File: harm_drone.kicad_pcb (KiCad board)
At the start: 2 copper layers, 90 x 40 mm, 0 parts

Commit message: initial PCB draft!
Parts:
- added C1: 0.1uF, Capacitor_SMD:C_0805_2012Metric, F.Cu at (131.9, 96.5)
- added C10: 22uF, Capacitor_SMD:C_0805_2012Metric, F.Cu at (112.4, 86.0)
- added C11: 22uF, Capacitor_SMD:C_0805_2012Metric, F.Cu at (112.4, 89.0)
- added C12: 47pF, Capacitor_SMD:C_0805_2012Metric, F.Cu at (116.9, 84.5)
- added C13: 47pF, Capacitor_SMD:C_0805_2012Metric, F.Cu at (116.9, 87.5)
- added C14: 1uF, Capacitor_SMD:C_0805_2012Metric, F.Cu at (116.9, 90.5)
- added C15: 10uF, Capacitor_SMD:C_0805_2012Metric, F.Cu at (131.9, 99.1)
- added C16: 0.1uF, Capacitor_SMD:C_0805_2012Metric, F.Cu at (132.0, 101.5)
- added C17: 0.1uF, Capacitor_SMD:C_0805_2012Metric, F.Cu at (140.9, 105.5)
- added C18: 10uF, Capacitor_SMD:C_0805_2012Metric, F.Cu at (143.4, 105.5)
- added C19: 10uF, Capacitor_SMD:C_0805_2012Metric, F.Cu at (144.4, 90.5)
- added C2: 10uF, Capacitor_SMD:C_0805_2012Metric, F.Cu at (180.4, 95.0)
- added C20: 0.1uF, Capacitor_SMD:C_0805_2012Metric, F.Cu at (141.9, 90.5)
- added C21: 10uF, Capacitor_SMD:C_0805_2012Metric, F.Cu at (135.4, 90.5)
- added C22: 0.1uF, Capacitor_SMD:C_0805_2012Metric, F.Cu at (137.9, 90.5)
- added C23: 10uF, Capacitor_SMD:C_0805_2012Metric, F.Cu at (186.4, 113.0)
- added C24: 0.1uF, Capacitor_SMD:C_0805_2012Metric, F.Cu at (186.4, 116.0)
- added C3: 0.1uF, Capacitor_SMD:C_0805_2012Metric, F.Cu at (180.4, 98.0)
- added C4: 0.1uF, Capacitor_SMD:C_0805_2012Metric, F.Cu at (180.4, 101.0)
- added C5: 10uF, Capacitor_SMD:C_0805_2012Metric, F.Cu at (180.4, 104.0)
- added C6: 1uF, Capacitor_SMD:C_0805_2012Metric, F.Cu at (128.9, 83.0)
- added C7: 1uF, Capacitor_SMD:C_0805_2012Metric, F.Cu at (128.9, 86.0)
- added C8: 0.1uFCap, Capacitor_SMD:C_0805_2012Metric, F.Cu at (112.4, 80.0)
- added C9: 0.1uF, Capacitor_SMD:C_0805_2012Metric, F.Cu at (112.4, 83.0)
- added IC1: Microcontroller, group127:Microcontroller, F.Cu at (139.4, 98.0)
- added IC2: USB Hub, group127:USB-HUB, F.Cu at (171.9, 100.5)
- added IC3: SRAM, group127:SRAM, F.Cu at (157.8, 98.6)
- added IC4: LDO, group127:LDO, F.Cu at (130.3, 90.0)
- added J1: SYS_DEBUG, Connector_PinHeader_2.54mm:PinHeader_1x03_P2.54mm_Vertical, F.Cu at (149.4, 88.5)
- added J2: 2-Port USB, group127:USBPorts, F.Cu at (155.9, 110.8)
- added J3: 2-Port USB, group127:USBPorts, F.Cu at (172.4, 110.8)
- added J4: SD_Card, group127:SDCard, F.Cu at (196.9, 110.0)
- added J5: SPI2, Connector_PinHeader_2.54mm:PinHeader_1x04_P2.54mm_Vertical, F.Cu at (149.4, 106.0)
- added J6: SPI1, Connector_PinHeader_2.54mm:PinHeader_1x05_P2.54mm_Vertical, F.Cu at (144.4, 109.0)
- added J7: XT60-M, group127:XT60-M, F.Cu at (157.0, 86.9)
- added L1: 6.8uH, group127:Inductor, F.Cu at (102.9, 86.5)
- added R1: 2kOhm, Resistor_SMD:R_0805_2012Metric, F.Cu at (169.9, 93.0)
- added R10: 27ohm, Resistor_SMD:R_0805_2012Metric, F.Cu at (110.4, 100.5)
- added R11: 27ohm, Resistor_SMD:R_0805_2012Metric, F.Cu at (110.4, 103.5)
- added R12: 270ohm, Resistor_SMD:R_0805_2012Metric, F.Cu at (110.4, 106.5)
- added R13: 270ohm, Resistor_SMD:R_0805_2012Metric, F.Cu at (110.4, 109.4)
- added R14: 5.1kohm, Resistor_SMD:R_0805_2012Metric, F.Cu at (110.4, 112.3)
- added R15: 5.1kohm, Resistor_SMD:R_0805_2012Metric, F.Cu at (110.4, 115.3)
- added R2: 100k, Resistor_SMD:R_0805_2012Metric, F.Cu at (112.4, 92.0)
- added R3: 13.7k, Resistor_SMD:R_0805_2012Metric, F.Cu at (112.4, 94.9)
- added R4: 10kOhm, Resistor_SMD:R_0805_2012Metric, F.Cu at (198.9, 82.0)
- added R5: 10kOhm, Resistor_SMD:R_0805_2012Metric, F.Cu at (198.9, 85.0)
- added R6: 27, Resistor_SMD:R_0805_2012Metric, F.Cu at (198.9, 88.0)
- added R7: 10kOhm, Resistor_SMD:R_0805_2012Metric, F.Cu at (198.9, 90.9)
- added R8: 10kOhm, Resistor_SMD:R_0805_2012Metric, F.Cu at (198.9, 93.8)
- added R9: 10kOhm, Resistor_SMD:R_0805_2012Metric, F.Cu at (198.9, 96.8)
- added RXLED1: SM0805UBWC, KiCad0805:LEDC2012X110N, F.Cu at (118.4, 95.5)
- added S1: KSR221GLFS, group127:Button, F.Cu at (125.4, 99.7)
- added S2: Switch, JS102011SAQN:SW_JS102011SAQN, F.Cu at (138.9, 118.0)
- added TXLED1: SM0805UBWC, KiCad0805:LEDC2012X110N, F.Cu at (118.4, 98.8)
- added U1: LMR51430, Package_TO_SOT_SMD:SOT-23-6, F.Cu at (103.8, 96.5)
- added U2: EEPROM, group127:EEPROM, F.Cu at (157.8, 105.1)
- added USB-C1: USB4110GFA, USB4110_GF_A:GCT_USB4110GFA, F.Cu at (121.4, 113.9)
- added USB2UART1: FT231XS-R, Package_SO:SSOP-20_3.9x8.7mm_P0.635mm, F.Cu at (122.8, 87.6)
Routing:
- net GND: vias 0 -> 9
- net 3V3: vias 0 -> 8
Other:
- board size 90 x 40 mm -> 110 x 40 mm
- copper layers 2 -> 4

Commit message: before differential routing
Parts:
- C8: value 0.1uFCap -> 0.1uF
- moved C11 73.9 mm to (186.0, 82.0), turned to 90 degrees
- moved R2 70.9 mm to (183.0, 86.0), turned to 90 degrees
- moved R3 70.8 mm to (183.0, 90.0), turned to -90 degrees
- moved C10 70.7 mm to (183.0, 82.0), turned to 90 degrees
- moved L1 70.6 mm to (173.5, 85.5), turned to 180 degrees
- moved U1 61.1 mm to (164.0, 86.5)
- moved C6 52.5 mm to (178.0, 101.5)
- moved C8 52.2 mm to (163.0, 93.0), turned to 90 degrees
- moved C9 51.6 mm to (164.0, 82.5), turned to 180 degrees
- moved C7 49.8 mm to (178.0, 94.5)
- moved IC4 48.3 mm to (178.0, 98.0), turned to 90 degrees
- moved C2 32.2 mm to (149.5, 104.0), turned to 180 degrees
- moved C3 31.1 mm to (149.5, 101.5), turned to 180 degrees
- moved IC3 27.7 mm to (135.5, 115.0)
- moved R6 25.7 mm to (186.5, 110.5)
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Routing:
- net 5V: track 0.00 -> 59.7 mm
- net Net-(J7-POS): track 0.00 -> 6.64 mm
- net Net-(IC2-BUSPWR): track 0.00 -> 3.09 mm
- net GND: vias 9 -> 15
- net DP0: vias 0 -> 1
- net DM0: vias 0 -> 1
- net 3V3: vias 8 -> 14
- net /USB/DP4: vias 0 -> 1
- net /USB/DP3: vias 0 -> 1
- net /USB/DP2: vias 0 -> 1
- net /USB/DP1: vias 0 -> 1
- net /USB/DM4: vias 0 -> 1
- net /USB/DM3: vias 0 -> 1
- net /USB/DM2: vias 0 -> 1
- net /USB/DM1: vias 0 -> 1

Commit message: namespace change
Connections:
- net /USB/DM1 renamed /USB/D1-
- net /USB/DM2 renamed /USB/D2-
- net /USB/DM3 renamed /USB/D3-
- net /USB/DM4 renamed /USB/D4-
- net /USB/DP1 renamed /USB/D1+
- net /USB/DP2 renamed /USB/D2+
- net /USB/DP3 renamed /USB/D3+
- net /USB/DP4 renamed /USB/D4+
- net DM0 renamed D0-
- net DP0 renamed D0+

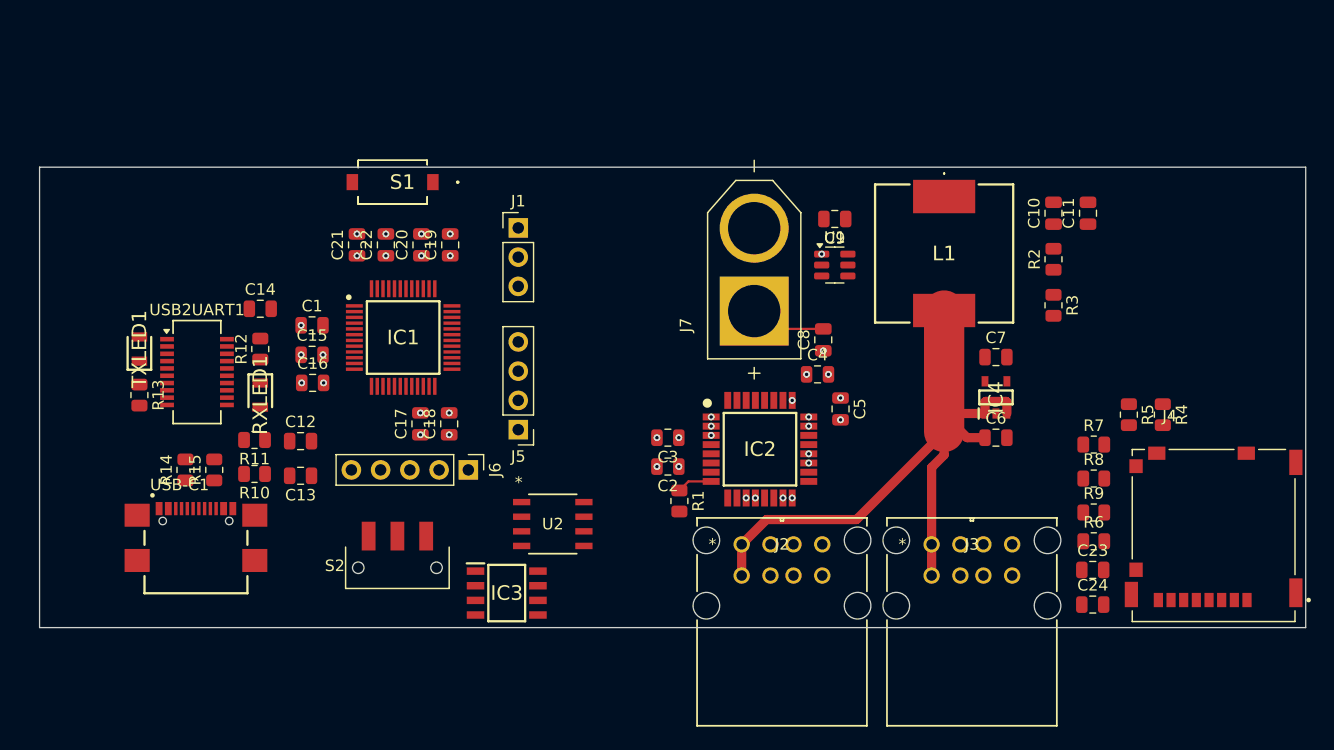
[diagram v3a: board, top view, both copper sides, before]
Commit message: add PWM LED
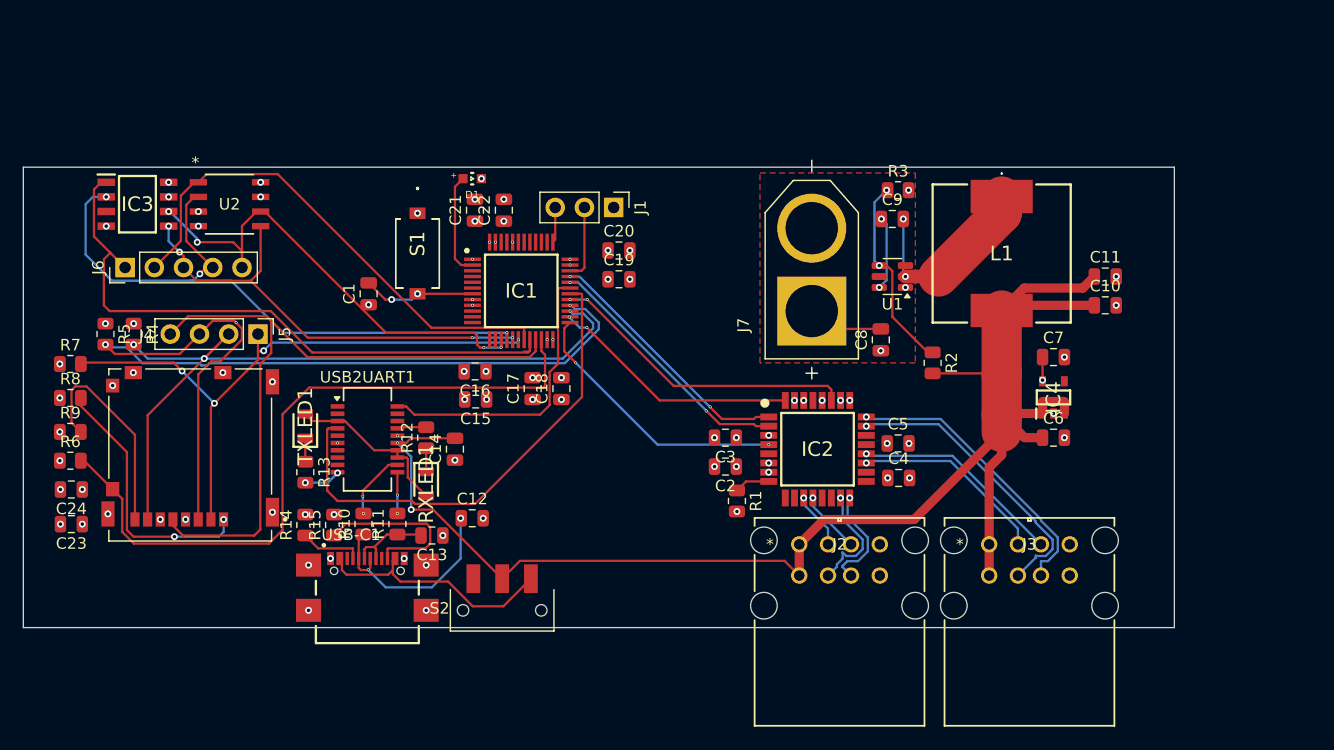
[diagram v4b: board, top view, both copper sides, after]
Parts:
- added D1: PWM_LED, group127:PWM_LED, F.Cu at (132.5, 79.0)
- moved R4 89.7 mm to (103.1, 92.5)
- moved C24 89.3 mm to (97.7, 106.0), turned to 180 degrees
- moved R5 89.2 mm to (100.6, 92.5)
- moved J4 89.2 mm to (108.0, 103.0)
- moved R6 89.2 mm to (97.6, 103.5)
- moved R7 89.2 mm to (97.6, 95.1)
- moved R8 89.2 mm to (97.6, 98.0)
- moved R9 89.2 mm to (97.6, 101.0)
- moved C23 88.8 mm to (97.7, 109.0), turned to 180 degrees
- moved IC3 46.6 mm to (103.4, 81.2)
- moved U2 39.5 mm to (111.4, 81.2)
- moved J6 34.6 mm to (102.3, 86.7), turned to 90 degrees
- moved J5 24.1 mm to (113.9, 92.5), turned to -90 degrees
- moved C14 20.9 mm to (131.0, 102.5), turned to 90 degrees
- moved C20 17.2 mm to (145.2, 85.2), turned to 0 degrees
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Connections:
- IC1 pad 2: unconnected-(IC1-PC13-Pad2) -> Net-(IC1-PC13)
- IC1 pad 22: unconnected-(IC1-PB11-Pad22) -> CARD_DETECT
- J4 pad CD: Net-(J4-PadCD) -> CARD_DETECT
- R6 pad 2: Net-(J4-PadCD) -> CARD_DETECT
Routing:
- net MOSI 2: track 0.00 -> 80.9 mm, vias 0 -> 3
- net 5V: track 59.7 -> 132.1 mm, vias 0 -> 2
- net MISO 2: track 0.00 -> 66.4 mm, vias 0 -> 3
- net SPI CLOCK 2: track 0.00 -> 62.8 mm
- net CARD_DETECT: track 0.00 -> 60.7 mm
- net MISO 1: track 0.00 -> 56.0 mm, vias 0 -> 3
- net CS SD Card: track 0.00 -> 54.3 mm, vias 0 -> 4
- net ~{CS} SRAM: track 0.00 -> 54.3 mm
- net CS EEPROM: track 0.00 -> 44.3 mm
- net RXD_USB2SERIAL: track 0.00 -> 42.7 mm
- net SPI CLOCK 1: track 0.00 -> 41.4 mm, vias 0 -> 4
- net MOSI 1: track 0.00 -> 40.3 mm, vias 0 -> 4
- net TSTPLL/48MCLK: track 0.00 -> 26.9 mm, vias 0 -> 2
- net /USB/D4-: track 0.00 -> 25.4 mm
- net TXD_USB2SERIAL: track 0.00 -> 25.4 mm
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- added copper zone on In1.Cu, net 3V3
- added copper zone on In2.Cu, net GND
- added copper zone on F.Cu, net Net-(J7-POS)
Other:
- board size 110 x 40 mm -> 100 x 40 mm

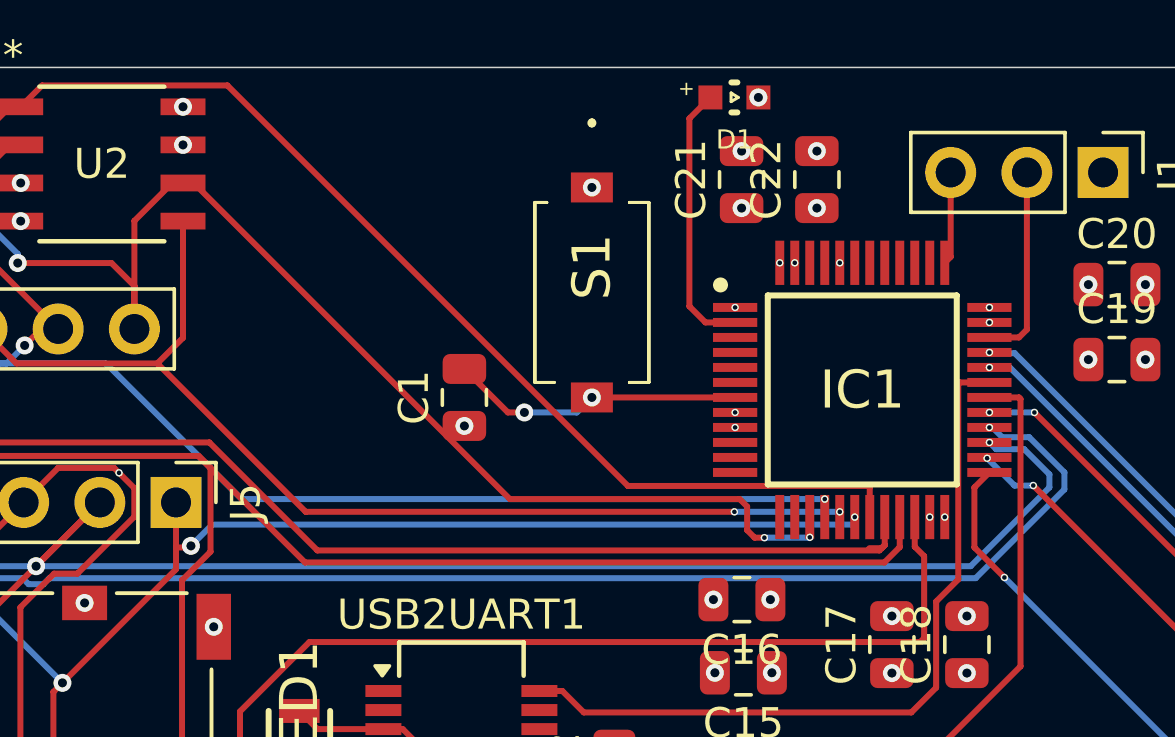
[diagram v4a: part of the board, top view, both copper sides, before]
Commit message: Fixed PCB mistakes
Moved Vias and one trace
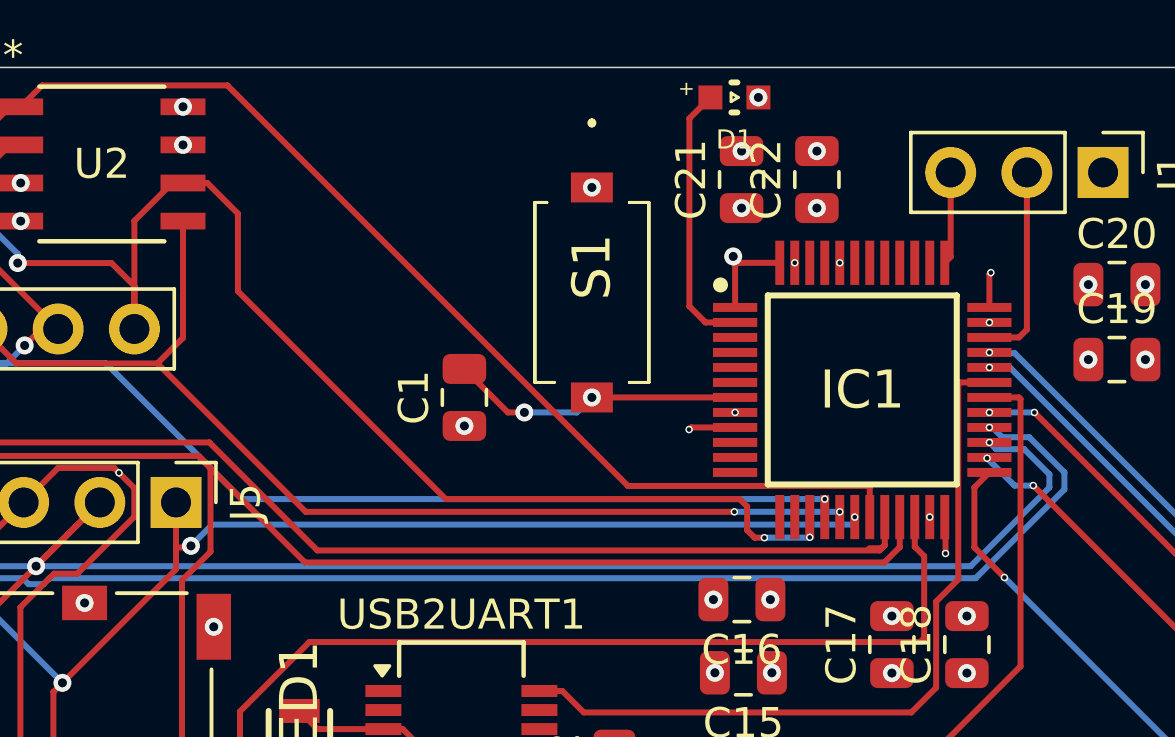
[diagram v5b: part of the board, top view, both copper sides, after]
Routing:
- net 3V3: track 2.10 -> 9.43 mm, vias 37 -> 36
- net SPI CLOCK 1: track 41.4 -> 42.9 mm
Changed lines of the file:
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@@
 		(descr "<B>WL-SMCW SMT Mono-color Chip LED Waterclear<Br><Br></B>Size: 0603, SMT, 2pins<Br>1.6x0.8x0.7mm(LXWXH)")
 		(property "Reference" "D1"
-			(at 0 -1.4064 360)
+			(at 0 -1.4064 0)
 			(layer "F.SilkS")
 			(effects
@@
 		)
 		(property "Value" "PWM_LED"
-			(at 0 1.2936 360)
+			(at 0 1.2936 0)
 			(layer "F.Fab")
 			(effects
@@
 		)
 		(property "Footprint" "group127:PWM_LED"
-			(at 0 0 360)
+			(at 0 0 0)
 			(layer "F.Fab")
 			(hide yes)
@@
 		)
 		(property "Datasheet" ""
-			(at 0 0 360)
+			(at 0 0 0)
 			(layer "F.Fab")
 			(hide yes)
@@
 		)
 		(property "Description" ""
-			(at 0 0 360)
+			(at 0 0 0)
 			(layer "F.Fab")
 			(hide yes)
@@
 		)
 		(fp_text user "+"
-			(at 1.6 0.3 360)
+			(at 1.6 0.3 0)
 			(layer "F.SilkS")
 			(effects
@@
 		)
 		(fp_text user "+"
-			(at 1.6 0.3 360)
+			(at 1.6 0.3 0)
 			(layer "F.Fab")
 			(effects
@@
 		(tags "capacitor")
 		(property "Reference" "C16"
-			(at 0 -1.68 360)
+			(at 0 -1.68 0)
 			(layer "F.SilkS")
 			(effects
@@
 		)
 		(property "Value" "0.1uF"
-			(at 0 1.68 360)
+			(at 0 1.68 0)
 			(layer "F.Fab")
 			(effects
@@
 		)
 		(fp_text user "${REFERENCE}"
-			(at 0 0 360)
+			(at 0 0 0)
 			(layer "F.Fab")
 			(effects
@@
 		(tags "capacitor")
 		(property "Reference" "C19"
-			(at 0 -1.68 360)
+			(at 0 -1.68 0)
 			(layer "F.SilkS")
 			(effects
@@
 		)
 		(property "Value" "10uF"
-			(at 0 1.68 360)
+			(at 0 1.68 0)
 			(layer "F.Fab")
 			(effects
@@
 		)
 		(fp_text user "${REFERENCE}"
-			(at 0 0 360)
+			(at 0 0 0)
 			(layer "F.Fab")
 			(effects
@@
 		(tags "capacitor")
 		(property "Reference" "C15"
-			(at 0 -1.68 360)
+			(at 0 -1.68 0)
 			(layer "F.SilkS")
 			(effects
@@
 		)
 		(property "Value" "10uF"
-			(at 0 1.68 360)
+			(at 0 1.68 0)
 			(layer "F.Fab")
 			(effects
@@
 		)
 		(fp_text user "${REFERENCE}"
-			(at 0 0 360)
+			(at 0 0 0)
 			(layer "F.Fab")
 			(effects
@@
 		(tags "capacitor")
 		(property "Reference" "C20"
-			(at 0 -1.68 360)
+			(at 0 -1.68 0)
 			(layer "F.SilkS")
 			(effects
@@
 		)
 		(property "Value" "0.1uF"
-			(at 0 1.68 360)
+			(at 0 1.68 0)
 			(layer "F.Fab")
 			(effects
@@
 		)
 		(fp_text user "${REFERENCE}"
-			(at 0 0 360)
+			(at 0 0 0)
 			(layer "F.Fab")
 			(effects
@@
 	)
 	(segment
+		(start 141 84.89)
+		(end 141.05 84.84)
+		(width 0.2)
+		(layer "F.Cu")
+		(net 3)
+	)
+	(segment
+		(start 131.06 90)
+		(end 130.99 90.07)
+		(width 0.2)
+		(layer "F.Cu")
+		(net 3)
+	)
+	(segment
 		(start 182.05 94.5)
 		(end 182.05 96.5)
@@
 	)
 	(segment
+		(start 132.672 84.512)
+		(end 132.46 84.3)
+		(width 0.2)
+		(layer "F.Cu")
+		(net 3)
+	)
+	(segment
 		(start 182.05 96.5)
 		(end 182.05 96.6)
@@
 		(net 3)
 	)
+	(segment
+		(start 132.524 90)
+		(end 131.06 90)
+		(width 0.2)
+		(layer "F.Cu")
+		(net 3)
+	)
+	(segment
+		(start 139.5375 94.2)
+		(end 139.5375 93.0135)
+		(width 0.2)
+		(layer "F.Cu")
+		(net 3)
+	)
+	(segment
+		(start 132.524 86)
+		(end 132.524 84.364)
+		(width 0.2)
+		(layer "F.Cu")
+		(net 3)
+	)
+	(segment
+		(start 132.524 84.364)
+		(end 132.46 84.3)
+		(width 0.2)
+		(layer "F.Cu")
+		(net 3)
+	)
+	(segment
+		(start 141 86)
+		(end 141 84.89)
+		(width 0.2)
+		(layer "F.Cu")
+		(net 3)
+	)
+	(segment
+		(start 134.012 84.512)
+		(end 132.672 84.512)
+		(width 0.2)
+		(layer "F.Cu")
+		(net 3)
+	)
+	(segment
+		(start 139.5375 93.0135)
+		(end 139.512 92.988)
+		(width 0.2)
+		(layer "F.Cu")
+		(net 3)
+	)
 	(via
 		(at 144.3 87.738)
@@
 	)
 	(via
-		(at 141 86)
+		(at 141.05 84.84)
 		(size 0.25)
 		(drill 0.15)
@@
 	)
 	(via
-		(at 132.524 86)
-		(size 0.25)
-		(drill 0.15)
+		(at 100.6375 91.5875)
+		(size 0.6)
+		(drill 0.3)
 		(layers "F.Cu" "B.Cu")
 		(net 3)
 	)
 	(via
-		(at 100.6375 91.5875)
+		(at 137.75 96.288)
 		(size 0.6)
 		(drill 0.3)
@@
 	)
 	(via
-		(at 137.75 96.288)
+		(at 165.3 98.262)
 		(size 0.6)
 		(drill 0.3)
@@
 	)
 	(via
-		(at 165.3 98.262)
+		(at 132.46 84.3)
 		(size 0.6)
 		(drill 0.3)
 		(layers "F.Cu" "B.Cu")
+		(free yes)
 		(net 3)
 	)
@@
 	)
 	(via
-		(at 132.524 90)
+		(at 130.99 90.07)
 		(size 0.25)
 		(drill 0.15)
@@
 	)
 	(via
-		(at 139.512 92.988)
+		(at 139.5375 94.2)
 		(size 0.25)
 		(drill 0.15)
@@
 	)
 	(via
-		(at 134.012 84.512)
-		(size 0.25)
-		(drill 0.15)
-		(layers "F.Cu" "B.Cu")
-		(net 3)
-	)
-	(via
 		(at 96.675 101)
 		(size 0.6)
@@
 	)
 	(segment
-		(start 114.1201 81.8518)
-		(end 114.4788 81.8518)
+		(start 132.925 93.425)
+		(end 133.175 93.675)
 		(width 0.2)
 		(layer "F.Cu")
@@
 	)
 	(segment
-		(start 114.4788 81.8518)
-		(end 125.015 92.388)
+		(start 114.9318 81.8518)
+		(end 115.95 82.87)
 		(width 0.2)
 		(layer "F.Cu")
@@
 	)
 	(segment
-		(start 133.175 93.675)
-		(end 133.5 93.675)
+		(start 112.5 86.7168)
+		(end 112.5 83.1132)
 		(width 0.2)
 		(layer "F.Cu")
@@
 	)
 	(segment
-		(start 132.925 92.636959)
-		(end 132.925 93.425)
+		(start 115.95 82.87)
+		(end 115.95 85.46)
 		(width 0.2)
 		(layer "F.Cu")
@@
 	)
 	(segment
-		(start 132.676041 92.388)
-		(end 132.925 92.636959)
+		(start 114.1201 81.8518)
+		(end 114.9318 81.8518)
 		(width 0.2)
 		(layer "F.Cu")
@@
 	)
 	(segment
-		(start 125.015 92.388)
+		(start 122.878 92.388)
 		(end 132.676041 92.388)
 		(width 0.2)
@@
 	)
 	(segment
+		(start 112.5 83.1132)
+		(end 113.7614 81.8518)
+		(width 0.2)
+		(layer "F.Cu")
+		(net 48)
+	)
+	(segment
 		(start 112.5 86.7168)
-		(end 112.5 83.1132)
+		(end 112.5 85.2832)
 		(width 0.2)
 		(layer "F.Cu")
@@
 	)
 	(segment
-		(start 112.5 83.1132)
-		(end 113.7614 81.8518)
+		(start 132.676041 92.388)
+		(end 132.925 92.636959)
 		(width 0.2)
 		(layer "F.Cu")
@@
 	)
 	(segment
-		(start 112.5 86.7168)
-		(end 112.5 85.2832)
+		(start 133.175 93.675)
+		(end 133.5 93.675)
+		(width 0.2)
+		(layer "F.Cu")
+		(net 48)
+	)
+	(segment
+		(start 115.95 85.46)
+		(end 122.878 92.388)
+		(width 0.2)
+		(layer "F.Cu")
+		(net 48)
+	)
+	(segment
+		(start 132.925 92.636959)
+		(end 132.925 93.425)
 		(width 0.2)
 		(layer "F.Cu")
@@
 		(width 0.2)
 		(layer "F.Cu")
-		(net 48)
-	)
-	(segment
-		(start 132.925 93.425)
-		(end 133.175 93.675)
-		(width 0.2)
-		(layer "F.Cu")

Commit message: before model updates
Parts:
- added H1: MountingHole, MountingHole:MountingHole_3.2mm_M3, F.Cu at (114.8, 98.5)
- added H2: MountingHole, MountingHole:MountingHole_3.2mm_M3, F.Cu at (172.2, 98.5)
- USB-C1: footprint USB4110_GF_A:GCT_USB4110GFA -> group127:GCT_USB4110GFA
- moved C23 7.50 mm to (97.7, 116.5)
- moved C24 7.50 mm to (97.7, 113.5)
- moved R6 7.25 mm to (97.6, 110.8)
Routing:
- net CARD_DETECT: track 60.7 -> 57.2 mm
- net 5V: track 132.1 -> 133.5 mm
